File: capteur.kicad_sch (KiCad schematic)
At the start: 17 parts, among them U1 MAX86141ENP+T

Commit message: Update for JLC parts
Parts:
- removed C7: 22µ, Capacitor_SMD:C_0805_2012Metric, symbol Device:C
- removed D1, D2, D3: CT DBLP31.12-6C5D-56-J6U6-20-R18, Local:CTDBLP31126C5D56J6U620R18, symbol Device:LED
- added D1, D2, D3: JNJ-LTJG0106W15, LED_SMD:LED_PLCC_2835, symbol LED_project:LED
- C6: value 22µ -> 100n; JLCPCB Part # C907991 -> C1711; manf# GRM21BZ71A226ME15L -> CL21B104KBCNNNC
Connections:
- net +1.8V: now also C6.1
- net +3.3V: no longer C6.1, U1.A1 (VLED)
- net +3.3V_LED: now also U1.A1 (VLED), D1.1 (A), D2.1 (A), D3.1 (A)
- net at U1.C1 (LED2_DRV): now also D2.2 (K)
- net at U1.D1 (LED1_DRV): now also D1.2 (K)
- net at U1.B1 (LED3_DRV): now also D3.2 (K)

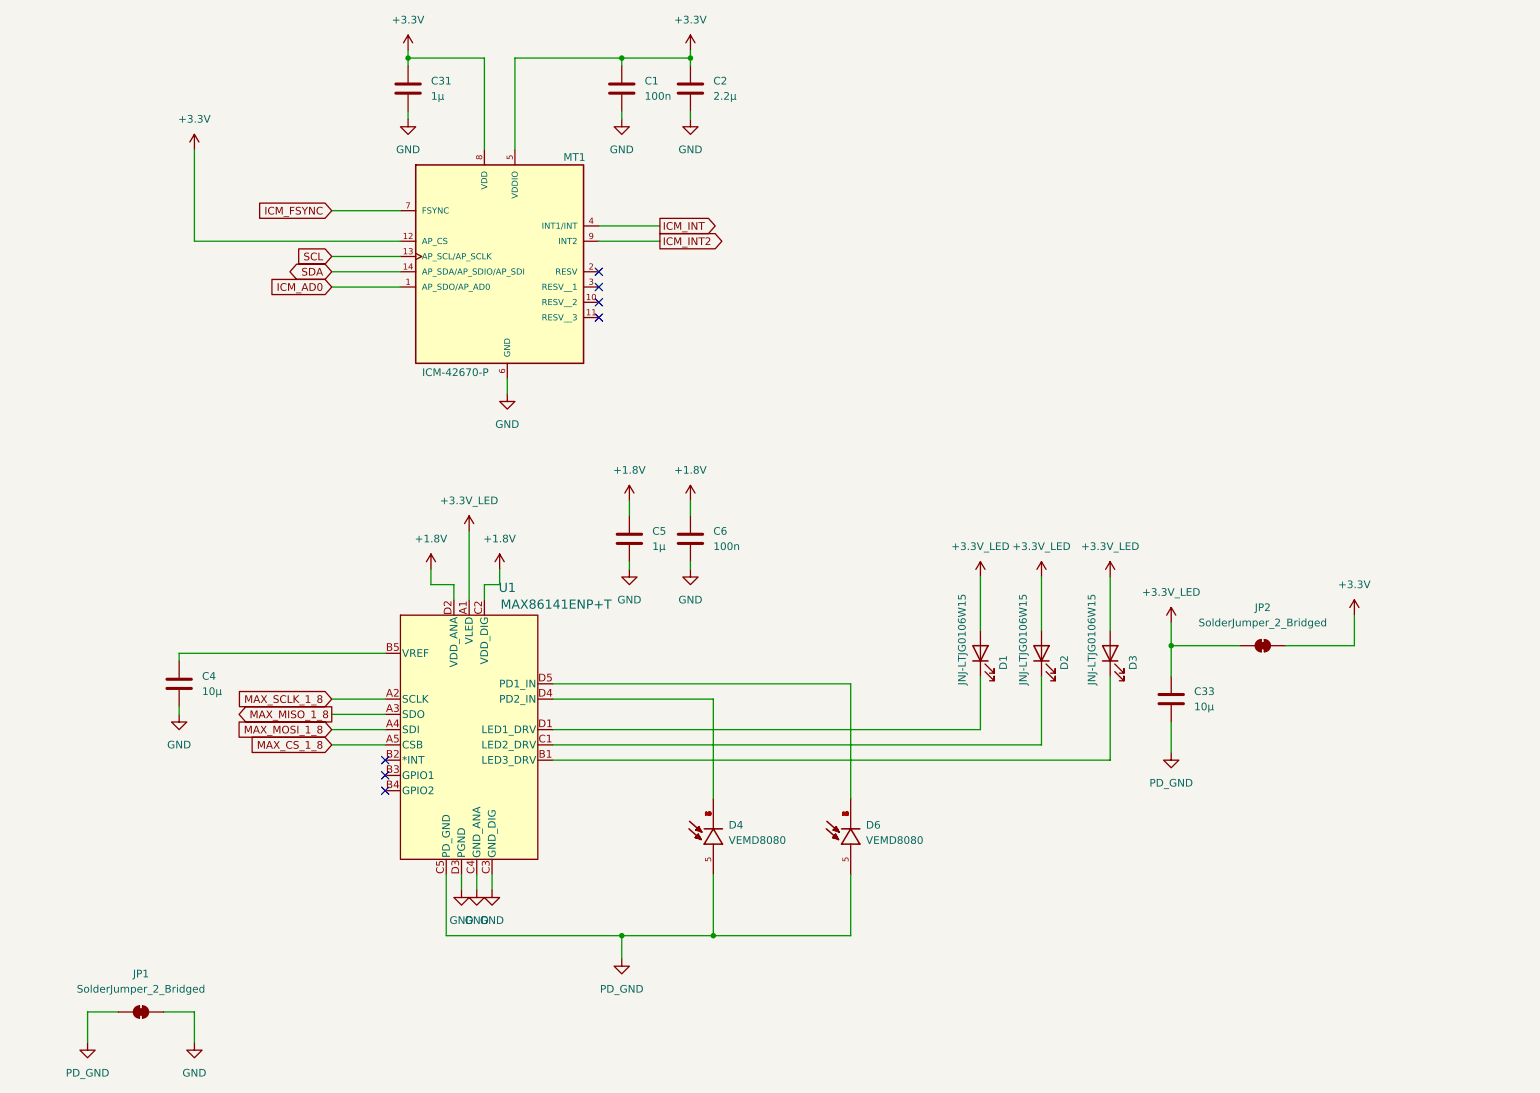
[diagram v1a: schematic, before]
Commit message: Add red and IR LED for capter
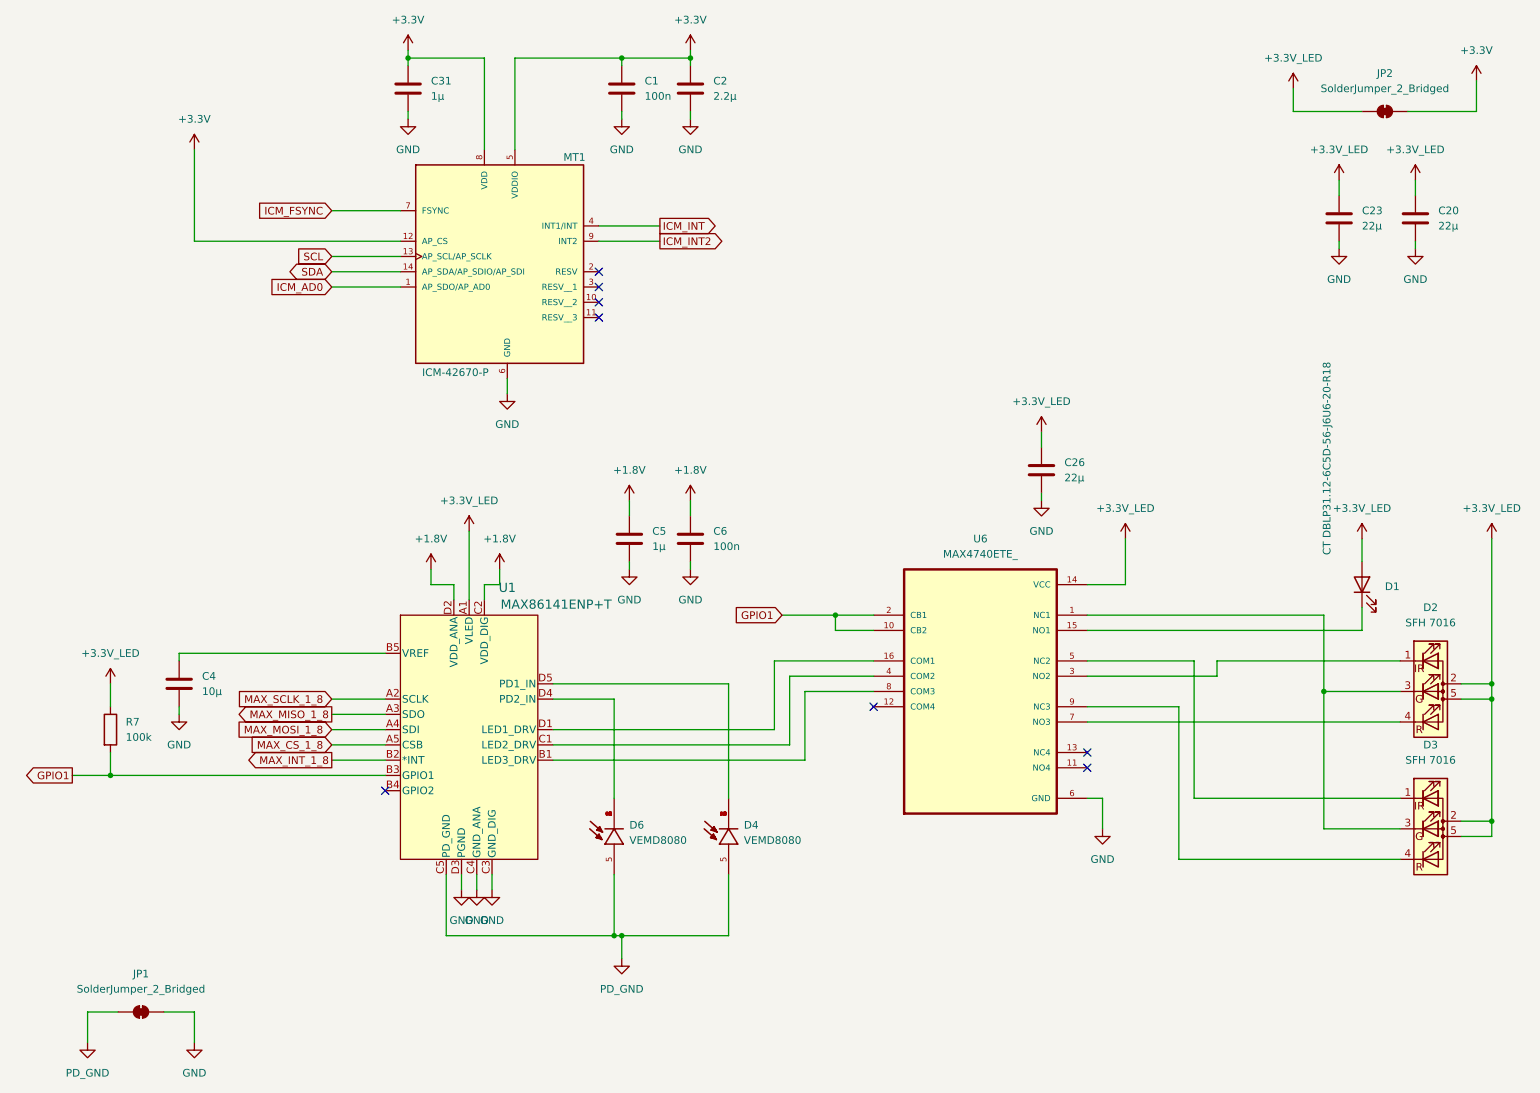
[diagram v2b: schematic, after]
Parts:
- removed C33: 10µ, Capacitor_SMD:C_0805_2012Metric, symbol Device:C
- removed D2, D3: JNJ-LTJG0106W15, LED_SMD:LED_PLCC_2835, symbol LED_project:LED
- added C20, C23, C26: 22µ, Capacitor_SMD:C_0805_2012Metric, symbol Device:C
- added D2, D3: SFH 7016, Local:SFH7016, symbol LED_project:SFH 7016
- added R7: 100k, Resistor_SMD:R_0805_2012Metric, symbol Device:R
- added U6: MAX4740ETE_, Local:QFN50P300X300X80-17N, symbol MAX4740ETE_:MAX4740ETE_
- D1: value JNJ-LTJG0106W15 -> CT DBLP31.12-6C5D-56-J6U6-20-R18; footprint LED_SMD:LED_PLCC_2835 -> Local:CTDBLP31126C5D56J6U620R18; JLCPCB Part # C7500147 -> C5344735; manf# JNJ-LTJG0106W15 -> CT DBLP31.12-6C5D-56-J6U6-20-R18
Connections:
- net +3.3V_LED: now also C20.1, C23.1, C26.1, D2.2 (A), D2.5 (A), D3.2 (A), D3.5 (A), R7.1, U6.14 (VCC)
- net GND: now also C20.2, C23.2, C26.2, U6.17 (GND), U6.6 (GND)
- net at D6.1, D6.2, D6.3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: now also U1.D4 (PD2_IN); no longer U1.D5 (PD1_IN)
- net at D1.2 (K): now also U6.15 (NO1); no longer U1.D1 (LED1_DRV)
- net at U1.B1 (LED3_DRV): now also U6.8 (COM3)
- net MAX_INT_1_8: now reaches U1.B2 (*INT)
- net GPIO1: now reaches U1.B3 (GPIO1)
- net GPIO1: now also R7.2, U6.10 (CB2), U6.2 (CB1)
- net at U1.C1 (LED2_DRV): now also U6.4 (COM2)
- net at D4.1, D4.2, D4.3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: now also U1.D5 (PD1_IN); no longer U1.D4 (PD2_IN)
- new net: D2.3 (GK), D3.3 (GK), U6.1 (NC1)
- new net: U1.D1 (LED1_DRV), U6.16 (COM1)
- new net: D2.1 (RK), U6.3 (NO2)
- new net: D3.1 (RK), U6.5 (NC2)
- new net: D2.4 (BK), U6.7 (NO3)
- new net: D3.4 (BK), U6.9 (NC3)
- no-connect marks 7 -> 8
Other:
- moved on the sheet: D4, D6, JP2

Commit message: some PCB correction
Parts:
- D1: JLCPCB Part # C5344735 -> C5603826
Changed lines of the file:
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@@
 			)
 		)
-		(property "Sim.Enable" ""
-			(at 189.23 129.54 0)
-			(effects
-				(font
-					(size 1.27 1.27)
-				)
-				(hide yes)
-			)
-		)
 		(pin "8"
 		)
@@
 			)
 		)
-		(property "Sim.Enable" ""
-			(at 261.62 50.8 0)
-			(effects
-				(font
-					(size 1.27 1.27)
-				)
-				(hide yes)
-			)
-		)
 		(pin "2"
 		)
@@
 			)
 		)
-		(property "Sim.Enable" ""
-			(at 128.27 152.4 90)
-			(effects
-				(font
-					(size 1.27 1.27)
-				)
-				(hide yes)
-			)
-		)
 		(pin "5"
 		)
@@
 			)
 		)
-		(property "Sim.Enable" ""
-			(at 199.39 92.71 0)
-			(effects
-				(font
-					(size 1.27 1.27)
-				)
-				(hide yes)
-			)
-		)
 		(pin "2"
 		)
@@
 			)
 		)
-		(property "Sim.Enable" ""
-			(at 49.53 182.88 0)
-			(effects
-				(font
-					(size 1.27 1.27)
-				)
-				(hide yes)
-			)
-		)
 		(pin "1"
 		)
@@
 			)
 		)
-		(property "Sim.Enable" ""
-			(at 130.81 104.14 0)
-			(effects
-				(font
-					(size 1.27 1.27)
-				)
-				(hide yes)
-			)
-		)
 		(pin "2"
 		)
@@
 			)
 		)
-		(property "Sim.Enable" ""
-			(at 55.88 128.27 0)
-			(effects
-				(font
-					(size 1.27 1.27)
-				)
-				(hide yes)
-			)
-		)
 		(pin "2"
 		)
@@
 			)
 		)
-		(property "Sim.Enable" ""
-			(at 129.54 29.21 0)
-			(effects
-				(font
-					(size 1.27 1.27)
-				)
-				(hide yes)
-			)
-		)
 		(pin "2"
 		)
@@
 			)
 		)
-		(property "Sim.Enable" ""
-			(at 104.14 137.16 0)
-			(effects
-				(font
-					(size 1.27 1.27)
-				)
-				(hide yes)
-			)
-		)
 		(pin "A3"
 		)
@@
 			)
 		)
-		(property "Sim.Enable" ""
-			(at 264.16 129.54 0)
-			(effects
-				(font
-					(size 1.27 1.27)
-				)
-				(hide yes)
-			)
-		)
 		(pin "4"
 		)
@@
 			)
 		)
-		(property "Sim.Enable" ""
-			(at 140.97 104.14 0)
-			(effects
-				(font
-					(size 1.27 1.27)
-				)
-				(hide yes)
-			)
-		)
 		(pin "2"
 		)
@@
 			)
 		)
-		(property "Sim.Enable" ""
-			(at 44.45 135.89 0)
-			(effects
-				(font
-					(size 1.27 1.27)
-				)
-				(hide yes)
-			)
-		)
 		(pin "1"
 		)
@@
 			)
 		)
-		(property "Sim.Enable" ""
-			(at 147.32 152.4 90)
-			(effects
-				(font
-					(size 1.27 1.27)
-				)
-				(hide yes)
-			)
-		)
 		(pin "5"
 		)
@@
 			)
 		)
-		(property "Sim.Enable" ""
-			(at 93.98 29.21 0)
-			(effects
-				(font
-					(size 1.27 1.27)
-				)
-				(hide yes)
-			)
-		)
 		(pin "2"
 		)
@@
 			)
 		)
-		(property "Sim.Enable" ""
-			(at 264.16 152.4 0)
-			(effects
-				(font
-					(size 1.27 1.27)
-				)
-				(hide yes)
-			)
-		)
 		(pin "4"
 		)
@@
 			)
 		)
-		(property "Sim.Enable" ""
-			(at 109.22 58.42 0)
-			(effects
-				(font
-					(size 1.27 1.27)
-				)
-				(hide yes)
-			)
-		)
 		(pin "13"
 		)
@@
 			)
 		)
-		(property "Sim.Enable" ""
-			(at 248.92 50.8 0)
-			(effects
-				(font
-					(size 1.27 1.27)
-				)
-				(hide yes)
-			)
-		)
 		(pin "2"
 		)
@@
 			)
 		)
-		(property "Sim.Enable" ""
-			(at 140.97 29.21 0)
-			(effects
-				(font
-					(size 1.27 1.27)
-				)
-				(hide yes)
-			)
-		)
 		(pin "2"
 		)
@@
 			)
 		)
-		(property "JLCPCB Part #" "C5344735"
-			(at 252.73 111.76 90)
-			(effects
-				(font
-					(size 1.27 1.27)
-				)
-				(hide yes)
-			)
-		)
-		(property "Sim.Enable" ""
+		(property "JLCPCB Part #" "C5603826"
 			(at 252.73 111.76 90)
 			(effects
@@
 			(at 256.54 33.02 0)
 			(effects
-				(font
-					(size 1.27 1.27)
-				)
-				(hide yes)
-			)
-		)
-		(property "Sim.Enable" ""
-			(at 256.54 33.02 0)
-			(effects
